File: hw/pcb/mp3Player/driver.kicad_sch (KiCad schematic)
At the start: 6 parts, among them Q1 Q_NMOS, Q2 Q_PMOS, Q3 Q_PMOS, Q4 Q_NMOS, U1 TC4427xOA, U2 TC4427xOA

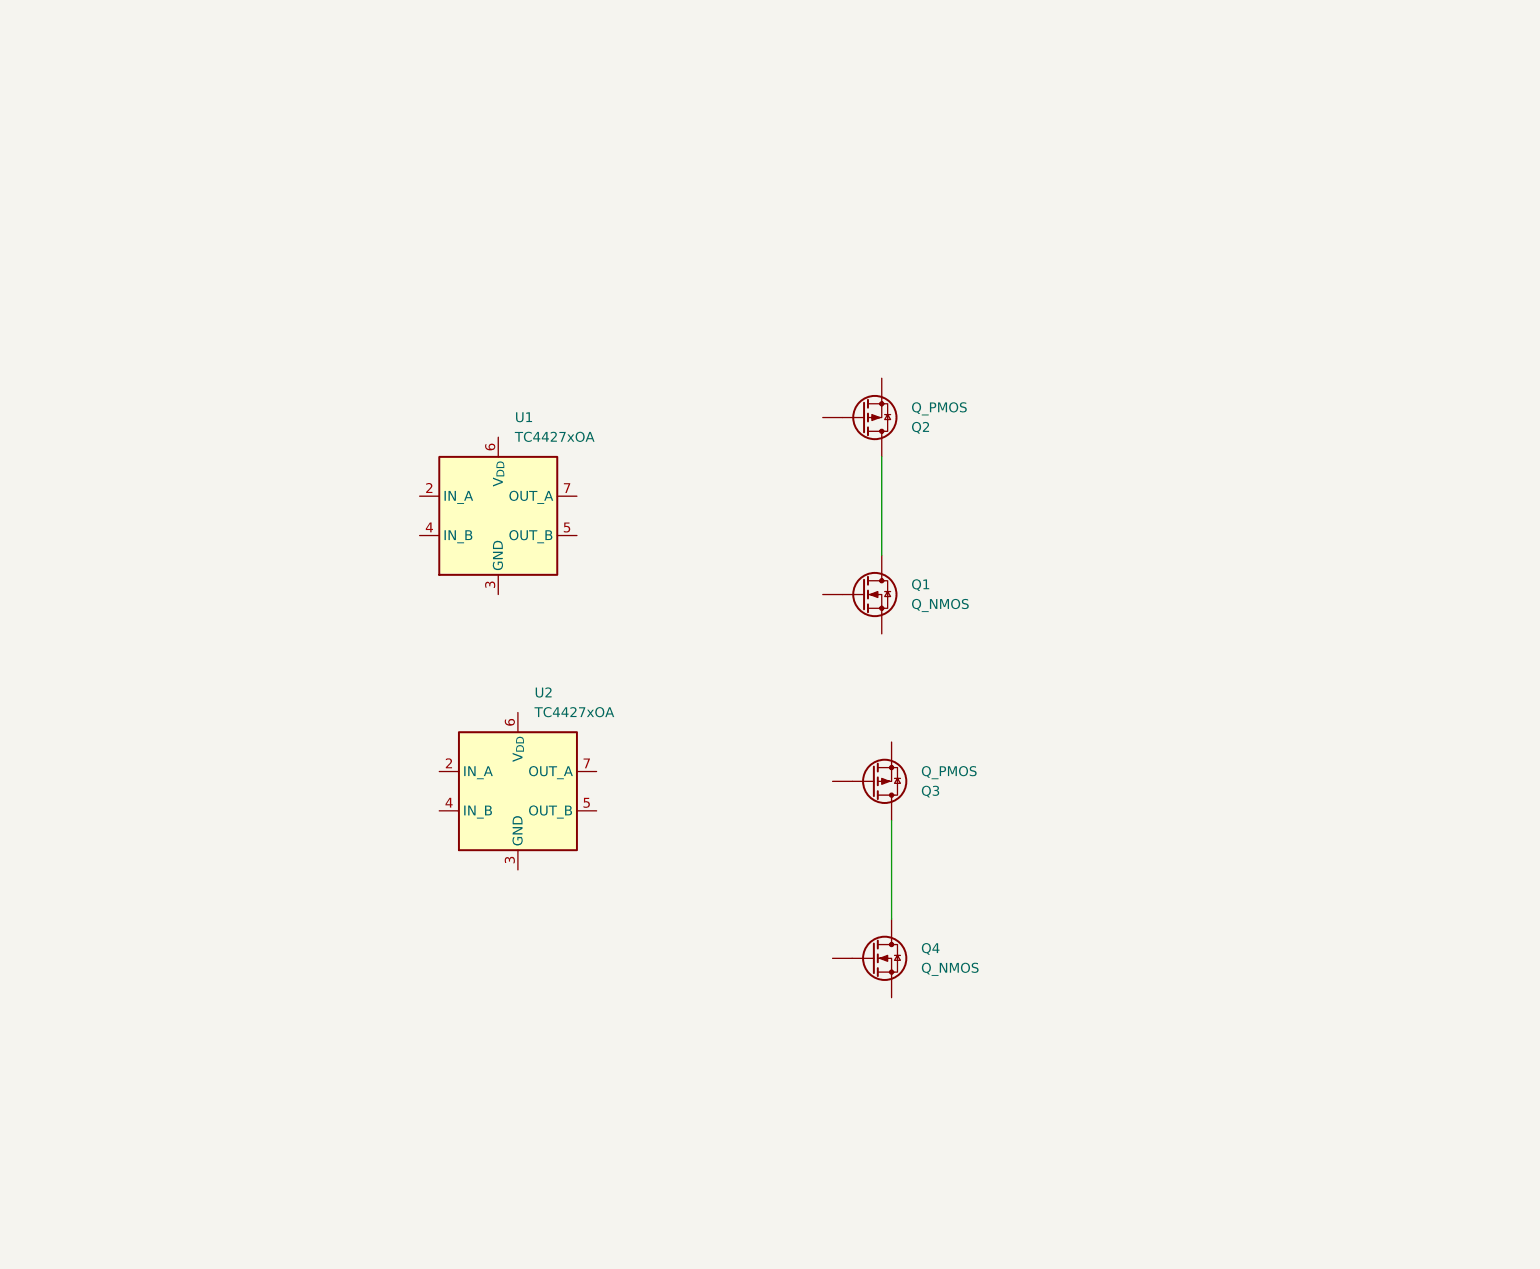
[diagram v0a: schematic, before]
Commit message: added pdm to pwm block for complementary half bridge driver
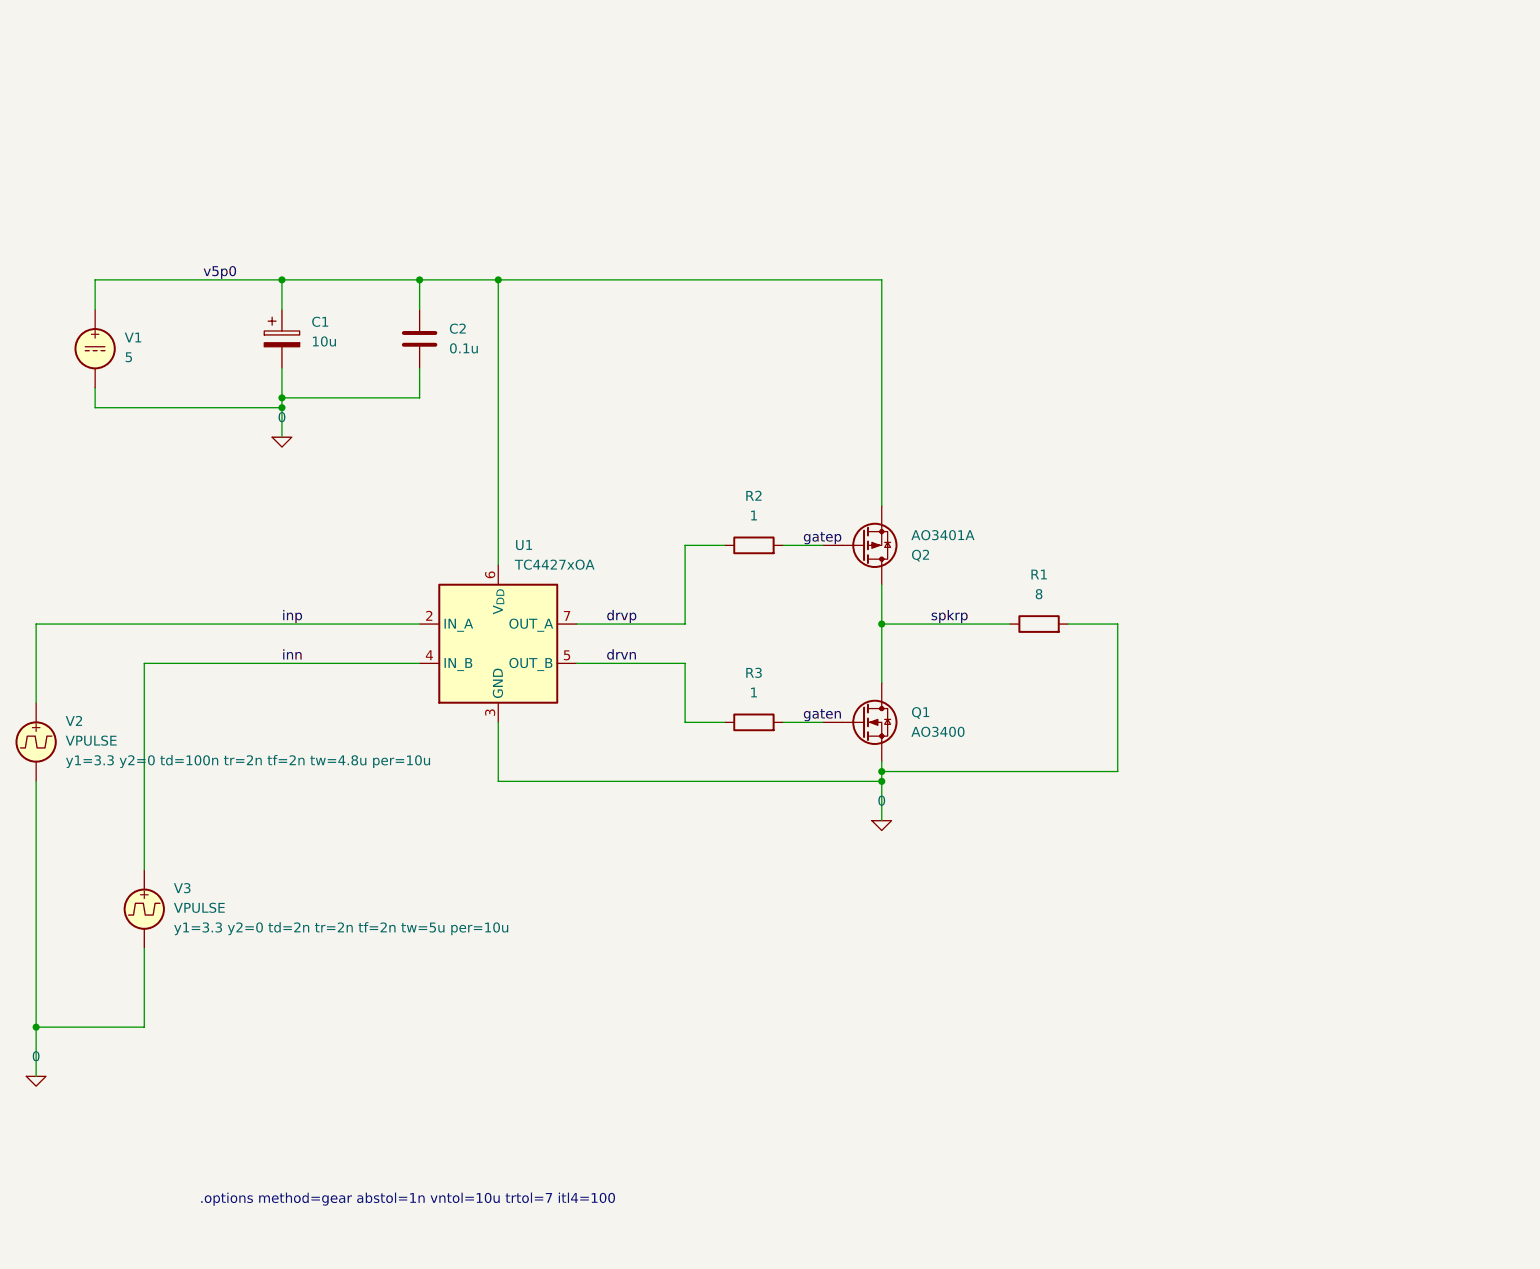
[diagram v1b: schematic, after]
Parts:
- removed Q3: Q_PMOS, symbol Device:Q_PMOS
- removed Q4: Q_NMOS, symbol Device:Q_NMOS
- removed U2: TC4427xOA, Package_SO:SOIC-8_3.9x4.9mm_P1.27mm, symbol Driver_FET:TC4427xOA
- added C1: 10u, Capacitor_SMD:C_1206_3216Metric, symbol Device:C_Polarized
- added C2: 0.1u, Capacitor_SMD:C_0603_1608Metric, symbol Device:C
- added R1: 8, symbol Device:R
- added R2, R3: 1, symbol Device:R
- added V1: 5, symbol Simulation_SPICE:VDC
- added V2, V3: VPULSE, symbol Simulation_SPICE:VPULSE
- Q1: value Q_NMOS -> AO3400; footprint (none) -> Package_TO_SOT_SMD:SOT-23
- Q2: value Q_PMOS -> AO3401A; footprint (none) -> Package_TO_SOT_SMD:SOT-23
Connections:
- net spkrp: now reaches Q1.D, Q2.D
- net spkrp: now also R1.1
- net gaten: now reaches Q1.G
- net gaten: now also R3.2
- net 0: now reaches Q1.S
- net 0: now also U1.3 (GND), C1.2, C2.2, R1.2, V1.2, V2.2, V3.2
- net inp: now reaches U1.2 (IN_A)
- net inp: now also V2.1
- net inn: now reaches U1.4 (IN_B)
- net inn: now also V3.1
- net drvn: now reaches U1.5 (OUT_B)
- net drvn: now also R3.1
- net v5p0: now reaches U1.6 (V_{DD})
- net v5p0: now also Q2.S, C1.1, C2.1, V1.1
- net drvp: now reaches U1.7 (OUT_A)
- net drvp: now also R2.1
- net gatep: now reaches Q2.G
- net gatep: now also R2.2
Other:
- note added: ".options method=gear abstol=1n vntol=10u trtol=7 itl4=100"
- moved on the sheet: Q1, Q2, U1

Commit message: updated pcb schematic
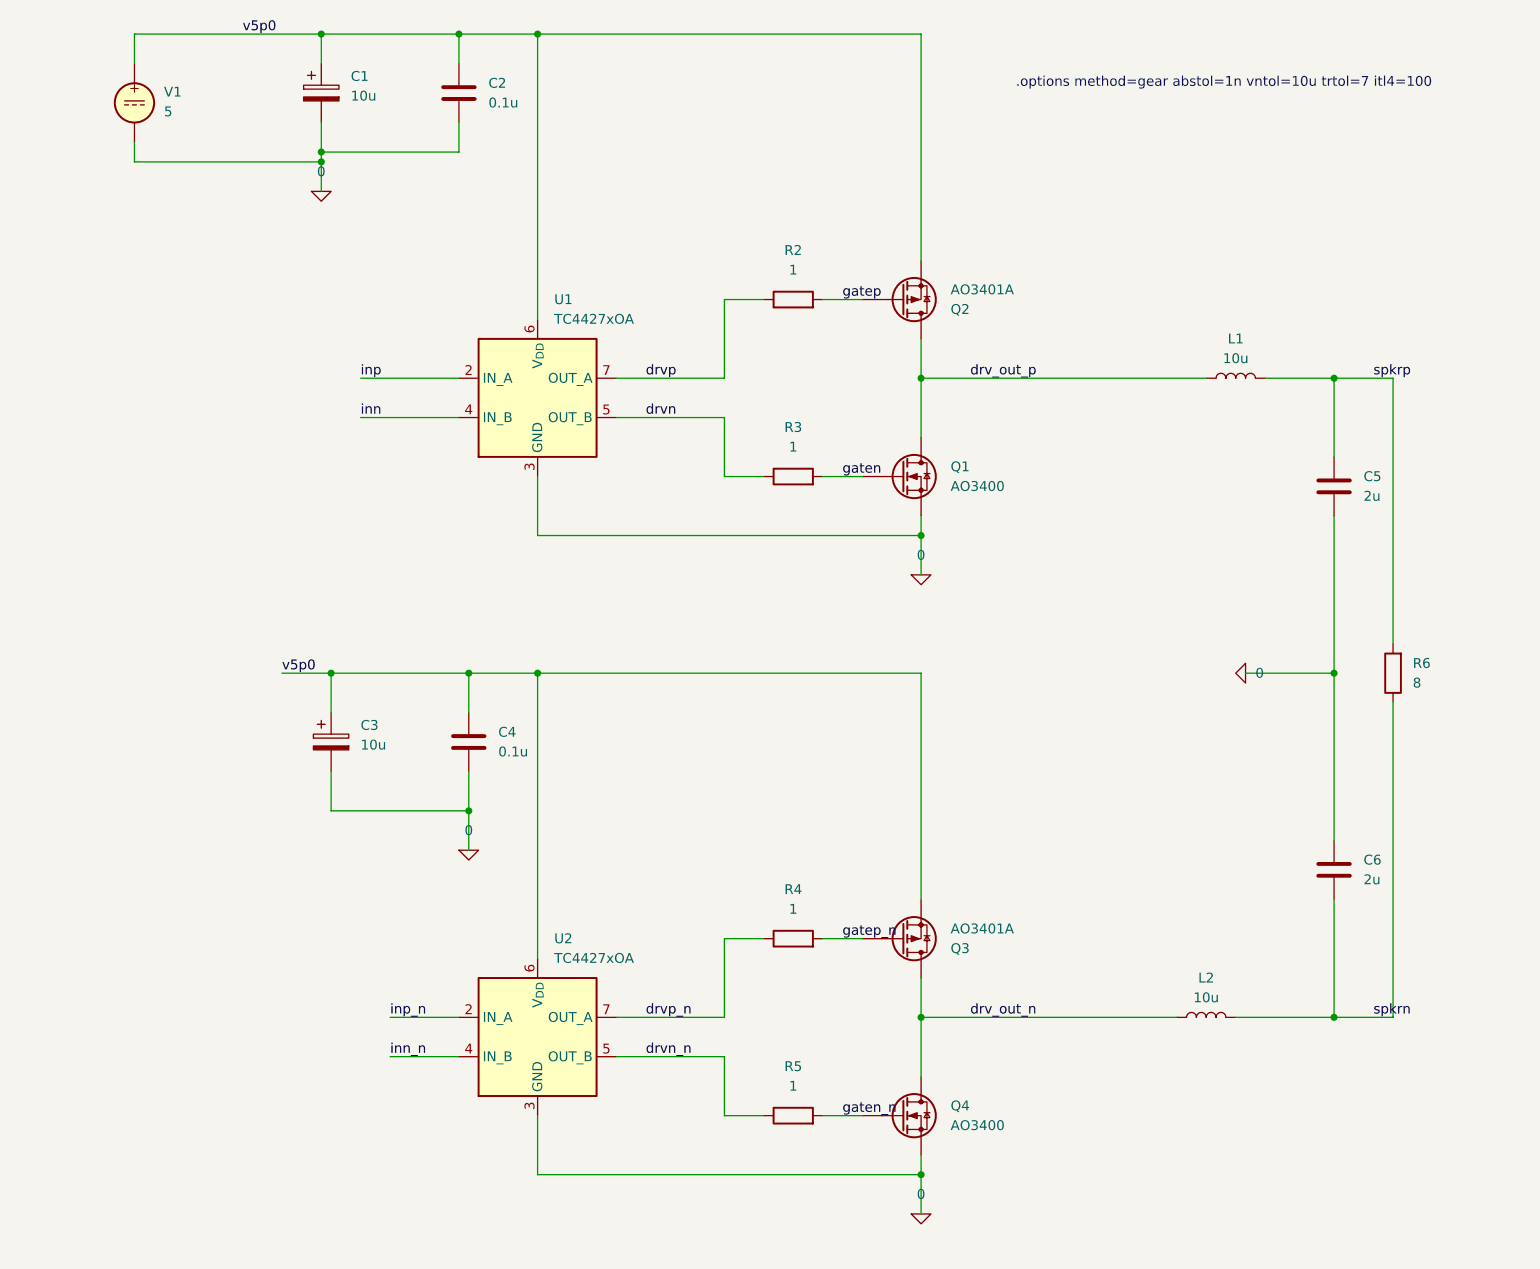
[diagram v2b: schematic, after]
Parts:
- removed R1: 8, symbol Device:R
- removed V2, V3: VPULSE, symbol Simulation_SPICE:VPULSE
- added C3: 10u, Capacitor_SMD:C_1206_3216Metric, symbol Device:C_Polarized
- added C4: 0.1u, Capacitor_SMD:C_0603_1608Metric, symbol Device:C
- added C5, C6: 2u, Capacitor_SMD:C_0603_1608Metric, symbol Device:C
- added L1, L2: 10u, symbol Device:L
- added Q3: AO3401A, Package_TO_SOT_SMD:SOT-23, symbol Device:Q_PMOS
- added Q4: AO3400, Package_TO_SOT_SMD:SOT-23, symbol Device:Q_NMOS
- added R4, R5: 1, symbol Device:R
- added R6: 8, symbol Device:R
- added U2: TC4427xOA, Package_SO:SOIC-8_3.9x4.9mm_P1.27mm, symbol Driver_FET:TC4427xOA
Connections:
- net 0: now also C3.2, C4.2, C5.2, C6.1, Q4.S, U2.3 (GND)
- net spkrp: now also C5.1, L1.2, R6.2; no longer Q1.D, Q2.D
- net v5p0: now also C3.1, C4.1, Q3.S, U2.6 (V_{DD})
- new net drv_out_n: L2.1, Q3.D, Q4.D
- new net drv_out_p: L1.1, Q1.D, Q2.D
- new net drvn_n: R5.1, U2.5 (OUT_B)
- new net drvp_n: R4.1, U2.7 (OUT_A)
- new net gaten_n: Q4.G, R5.2
- new net gatep_n: Q3.G, R4.2
- new net inn_n: U2.4 (IN_B)
- new net inp_n: U2.2 (IN_A)
- new net spkrn: C6.2, L2.2, R6.1
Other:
- moved on the sheet: C1, C2, Q1, Q2, R2, R3, U1, V1

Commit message: updates to pcb to supported updated rtl
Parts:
- removed V1: 5, symbol Simulation_SPICE:VDC
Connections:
- net 0 renamed GND
- net v5p0 renamed v5p0_drv
